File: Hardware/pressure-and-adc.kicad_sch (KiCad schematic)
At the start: 9 parts, among them Q1 Q_NPN_BEC, U6 LWP040-PSGLC-S, U7 ADS1015IDGSR, U8 INA350ABSIDDFR

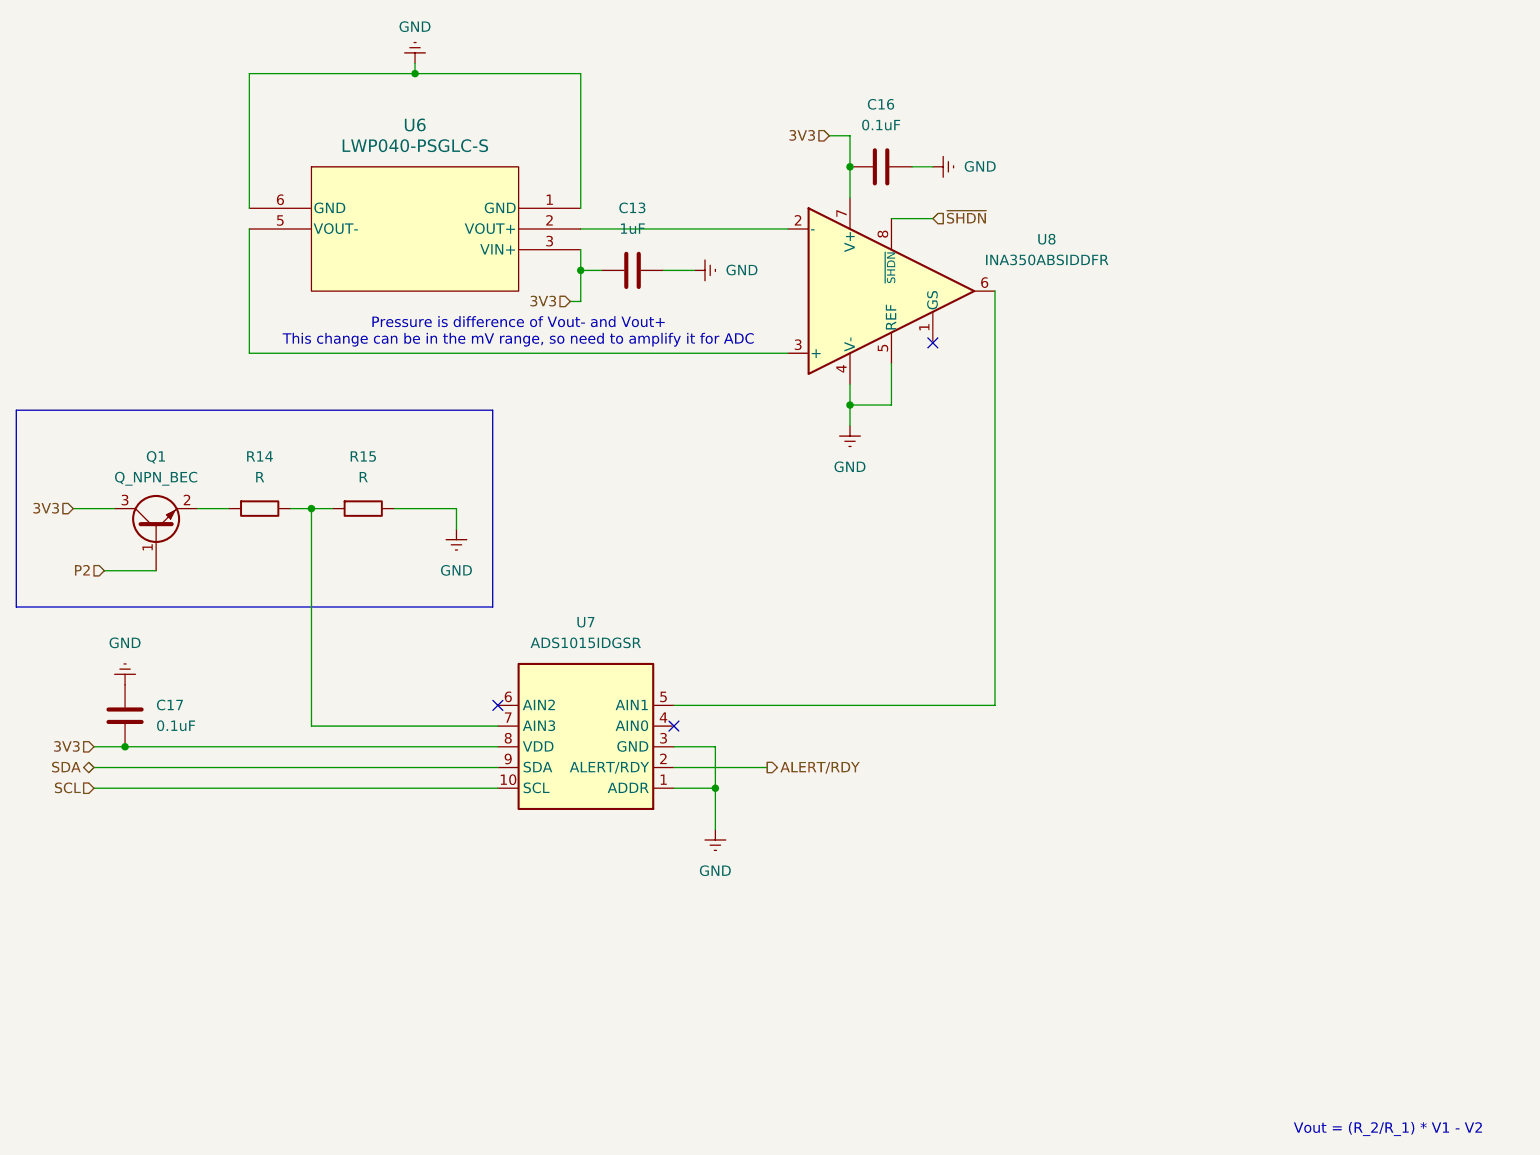
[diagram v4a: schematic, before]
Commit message: Initial OS architecture, and updated PCB work After a joint planning session, designed and architected OS structure: ``` src/ |- os: Audio, Accelerometer, Humidity, etc |- drivers: I2C interfaces, per-chip ```
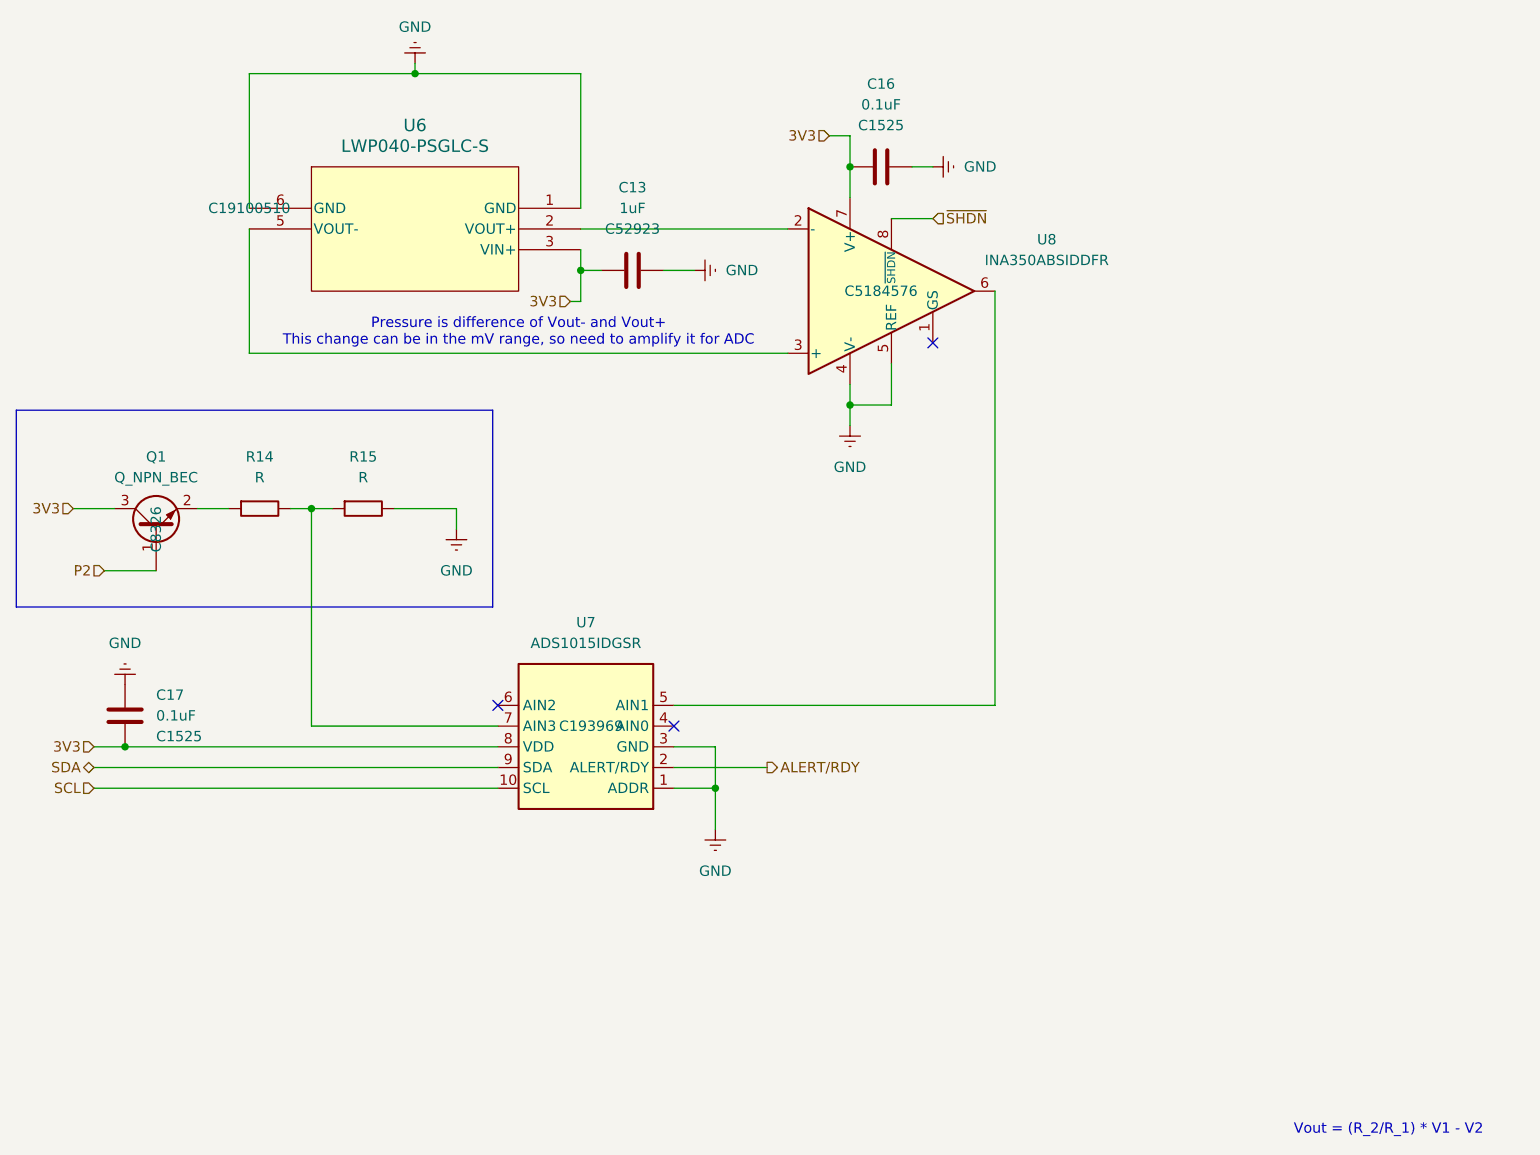
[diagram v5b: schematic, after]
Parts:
- C13: footprint Resistor_SMD:R_01005_0402Metric -> Capacitor_SMD:C_0402_1005Metric; symbol Peanut:C -> Peanut:C 1uF; LCSC (none) -> C52923
- C16, C17: footprint Resistor_SMD:R_01005_0402Metric -> Capacitor_SMD:C_0402_1005Metric; symbol Peanut:C -> Peanut:C 100nF; LCSC (none) -> C1525
- Q1: LCSC (none) -> C8326
- U6: LCSC (none) -> C19100510
- U7: LCSC (none) -> C193969
- U8: LCSC (none) -> C5184576
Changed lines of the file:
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@@
+			)
+		)
+		(property "LCSC" "C5184576"
+			(at 191.77 57.15 0)
+			(effects
+				(font
+					(size 1.27 1.27)
+				)
 			)
 		)
@@
 			)
 		)
+		(property "LCSC" "C19100510"
+			(at 114.3 46.99 0)
+			(effects
+				(font
+					(size 1.27 1.27)
+				)
+			)
+		)
 		(pin "1"
 		)
@@
 	)
 	(symbol
-		(lib_id "Peanut:C")
+		(lib_id "Peanut:C 100nF")
 		(at 99.06 109.22 180)
 		(unit 1)
@@
 		(fields_autoplaced yes)
 		(property "Reference" "C17"
-			(at 102.87 107.9499 0)
+			(at 102.87 106.6799 0)
 			(effects
 				(font
@@
 		)
 		(property "Value" "0.1uF"
-			(at 102.87 110.4899 0)
+			(at 102.87 109.2199 0)
 			(effects
 				(font
@@
 			)
 		)
-		(property "Footprint" "Resistor_SMD:R_01005_0402Metric"
+		(property "Footprint" "Capacitor_SMD:C_0402_1005Metric"
 			(at 98.0948 105.41 0)
 			(effects
@@
 			)
 		)
-		(property "Description" "Unpolarized capacitor"
+		(property "Description" "Capacitor 100nF"
 			(at 99.06 109.22 0)
 			(effects
@@
 				)
 				(hide yes)
+			)
+		)
+		(property "LCSC" "C1525"
+			(at 102.87 111.7599 0)
+			(effects
+				(font
+					(size 1.27 1.27)
+				)
+				(justify right)
 			)
 		)
@@
 			)
 		)
+		(property "LCSC" "C8326"
+			(at 102.87 86.36 0)
+			(effects
+				(font
+					(size 1.27 1.27)
+				)
+			)
+		)
 		(pin "3"
 		)
@@
 	)
 	(symbol
-		(lib_id "Peanut:C")
+		(lib_id "Peanut:C 100nF")
 		(at 191.77 41.91 90)
 		(unit 1)
@@
 		(fields_autoplaced yes)
 		(property "Reference" "C16"
+			(at 191.77 31.75 90)
+			(effects
+				(font
+					(size 1.27 1.27)
+				)
+			)
+		)
+		(property "Value" "0.1uF"
 			(at 191.77 34.29 90)
 			(effects
@@
 			)
 		)
-		(property "Value" "0.1uF"
-			(at 191.77 36.83 90)
-			(effects
-				(font
-					(size 1.27 1.27)
-				)
-			)
-		)
-		(property "Footprint" "Resistor_SMD:R_01005_0402Metric"
+		(property "Footprint" "Capacitor_SMD:C_0402_1005Metric"
 			(at 195.58 40.9448 0)
 			(effects
@@
 			)
 		)
-		(property "Description" "Unpolarized capacitor"
+		(property "Description" "Capacitor 100nF"
 			(at 191.77 41.91 0)
 			(effects
@@
 				)
 				(hide yes)
+			)
+		)
+		(property "LCSC" "C1525"
+			(at 191.77 36.83 90)
+			(effects
+				(font
+					(size 1.27 1.27)
+				)
 			)
 		)
@@
 			)
 		)
+		(property "LCSC" "C193969"
+			(at 156.21 110.49 0)
+			(effects
+				(font
+					(size 1.27 1.27)
+				)
+			)
+		)
 		(pin "7"
 		)
@@
 	)
 	(symbol
-		(lib_id "Peanut:C")
+		(lib_id "Peanut:C 1uF")
 		(at 161.29 54.61 90)
 		(unit 1)
@@
 		(fields_autoplaced yes)
 		(property "Reference" "C13"
+			(at 161.29 44.45 90)
+			(effects
+				(font
+					(size 1.27 1.27)
+				)
+			)
+		)
+		(property "Value" "1uF"
 			(at 161.29 46.99 90)
 			(effects
@@
 			)
 		)
-		(property "Value" "1uF"
-			(at 161.29 49.53 90)
-			(effects
-				(font
-					(size 1.27 1.27)
-				)
-			)
-		)
-		(property "Footprint" "Resistor_SMD:R_01005_0402Metric"
+		(property "Footprint" "Capacitor_SMD:C_0402_1005Metric"
 			(at 165.1 53.6448 0)
 			(effects
@@
 			)
 		)
+		(property "LCSC" "C52923"
+			(at 161.29 49.53 90)
+			(effects
+				(font
+					(size 1.27 1.27)
+				)
+			)
+		)

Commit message: Updates to PCB and ADC Schematics
- Swapped audio jack to correct pin (4P-DIP)
- Add LCSC numbers for all components
- Reroute some sensitive signal traces
- Add Board rev and author
- add 4x M2 mounting holes
- fixup some misc silkscreen, footprints, and component 3d models
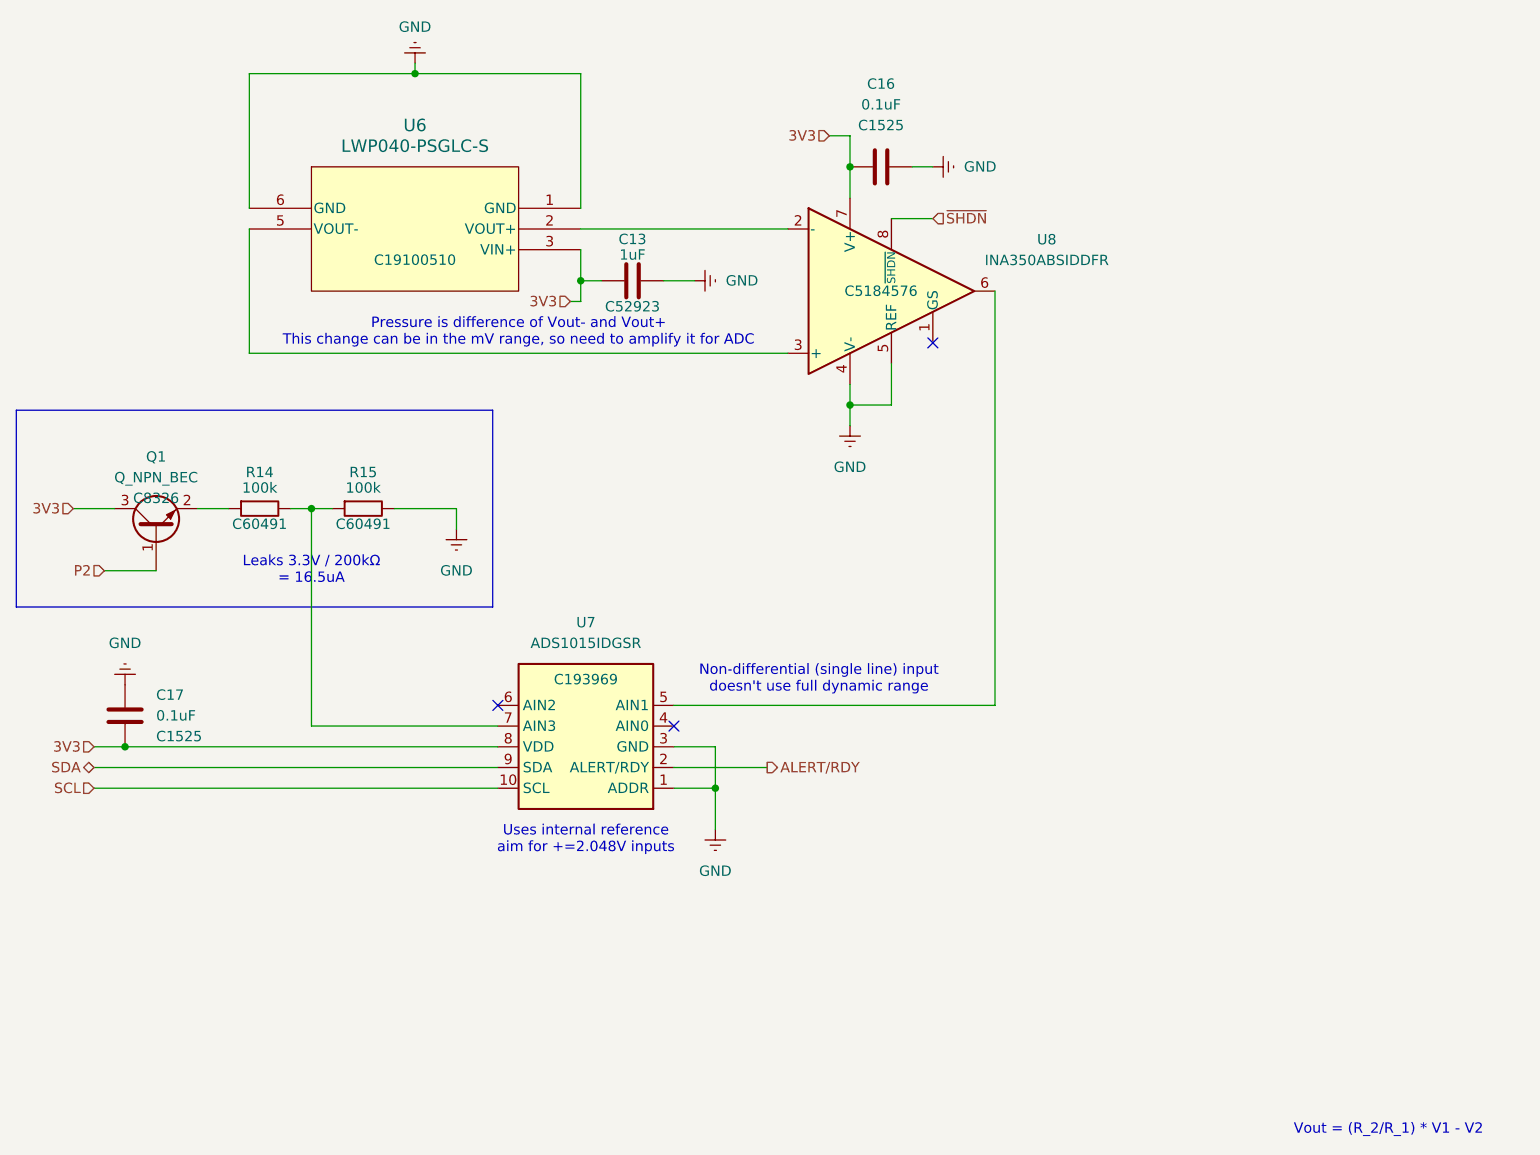
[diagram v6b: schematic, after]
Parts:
- R14, R15: value R -> 100k; symbol Peanut:R -> Peanut:R 100k; LCSC (none) -> C60491
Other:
- note added: "Leaks 3.3V / 200kΩ = 16.5uA"
- note added: "Non-differential (single line) input doesn't use full dynamic range"
- note added: "Uses internal reference aim for +=2.048V inputs"
- moved on the sheet: C13
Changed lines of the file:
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@@
-	)
-	(junction
-		(at 154.94 54.61)
-		(diameter 0)
-		(color 0 0 0 0)
 	)
 	(junction
@@
 	)
 	(junction
+		(at 154.94 55.88)
+		(diameter 0)
+		(color 0 0 0 0)
+	)
+	(junction
 		(at 121.92 83.82)
 		(diameter 0)
@@
 	(wire
 		(pts
+			(xy 154.94 55.88) (xy 154.94 58.42)
+		)
+		(stroke
+			(width 0)
+			(type default)
+		)
+	)
+	(wire
+		(pts
 			(xy 121.92 83.82) (xy 124.46 83.82)
 		)
@@
 	(wire
 		(pts
-			(xy 165.1 54.61) (xy 168.91 54.61)
+			(xy 165.1 55.88) (xy 168.91 55.88)
 		)
 		(stroke
@@
 	(wire
 		(pts
-			(xy 154.94 52.07) (xy 154.94 54.61)
-		)
-		(stroke
-			(width 0)
-			(type default)
-		)
-	)
-	(wire
-		(pts
 			(xy 193.04 48.26) (xy 198.12 48.26)
 		)
@@
 	(wire
 		(pts
-			(xy 154.94 54.61) (xy 157.48 54.61)
+			(xy 154.94 55.88) (xy 157.48 55.88)
 		)
 		(stroke
@@
 	(wire
 		(pts
-			(xy 154.94 54.61) (xy 154.94 58.42)
+			(xy 154.94 52.07) (xy 154.94 55.88)
 		)
 		(stroke
@@
 		(exclude_from_sim no)
 		(at 147.32 62.23 0)
+		(effects
+			(font
+				(size 1.27 1.27)
+			)
+		)
+	)
+	(text "Uses internal reference\naim for +=2.048V inputs"
+		(exclude_from_sim no)
+		(at 155.575 124.46 0)
+		(effects
+			(font
+				(size 1.27 1.27)
+			)
+		)
+	)
+	(text "Non-differential (single line) input\ndoesn't use full dynamic range"
+		(exclude_from_sim no)
+		(at 184.15 104.775 0)
+		(effects
+			(font
+				(size 1.27 1.27)
+			)
+		)
+	)
+	(text "Leaks 3.3V / 200kΩ\n= 16.5uA"
+		(exclude_from_sim no)
+		(at 121.92 91.44 0)
 		(effects
 			(font
@@
 	(symbol
 		(lib_id "Peanut:GND")
-		(at 168.91 54.61 90)
+		(at 168.91 55.88 90)
 		(unit 1)
 		(exclude_from_sim no)
@@
 		(fields_autoplaced yes)
 		(property "Reference" "#PWR033"
-			(at 175.26 54.61 0)
+			(at 175.26 55.88 0)
 			(effects
 				(font
@@
 		)
 		(property "Value" "GND"
-			(at 172.72 54.6099 90)
+			(at 172.72 55.8799 90)
 			(effects
 				(font
@@
 		)
 		(property "Footprint" ""
-			(at 168.91 54.61 0)
+			(at 168.91 55.88 0)
 			(effects
 				(font
@@
 		)
 		(property "Datasheet" ""
-			(at 168.91 54.61 0)
+			(at 168.91 55.88 0)
 			(effects
 				(font
@@
 		)
 		(property "Description" ""
-			(at 177.546 54.61 0)
+			(at 177.546 55.88 0)
 			(effects
 				(font
@@
 		(on_board yes)
 		(dnp no)
-		(fields_autoplaced yes)
 		(property "Reference" "U6"
 			(at 134.62 36.83 0)
@@
 		)
 		(property "LCSC" "C19100510"
-			(at 114.3 46.99 0)
+			(at 134.62 53.34 0)
 			(effects
 				(font
@@
 	)
 	(symbol
-		(lib_id "Peanut:R")
+		(lib_id "Peanut:R 100k")
 		(at 115.57 83.82 0)
 		(unit 1)
@@
 		(on_board yes)
 		(dnp no)
-		(fields_autoplaced yes)
 		(property "Reference" "R14"
-			(at 115.57 77.47 0)
-			(effects
-				(font
-					(size 1.27 1.27)
-				)
-			)
-		)
-		(property "Value" "R"
-			(at 115.57 80.01 0)
+			(at 115.57 79.375 0)
+			(effects
+				(font
+					(size 1.27 1.27)
+				)
+			)
+		)
+		(property "Value" "100k"
+			(at 115.57 81.28 0)
 			(effects
 				(font
@@
 				)
 				(hide yes)
+			)
+		)
+		(property "LCSC" "C60491"
+			(at 115.57 85.725 0)
+			(effects
+				(font
+					(size 1.27 1.27)
+				)
 			)
 		)
@@
 		(on_board yes)
 		(dnp no)
-		(fields_autoplaced yes)
 		(property "Reference" "Q1"
 			(at 102.87 77.47 90)
@@
 		)
 		(property "LCSC" "C8326"
-			(at 102.87 86.36 0)
+			(at 102.87 82.55 90)
 			(effects
 				(font
@@
 	)
 	(symbol
-		(lib_id "Peanut:R")
+		(lib_id "Peanut:R 100k")
 		(at 128.27 83.82 0)
 		(unit 1)
@@
 		(on_board yes)
 		(dnp no)
-		(fields_autoplaced yes)
 		(property "Reference" "R15"
-			(at 128.27 77.47 0)
-			(effects
-				(font
-					(size 1.27 1.27)
-				)
-			)
-		)
-		(property "Value" "R"
-			(at 128.27 80.01 0)
+			(at 128.27 79.375 0)
+			(effects
+				(font
+					(size 1.27 1.27)
+				)
+			)
+		)
+		(property "Value" "100k"
+			(at 128.27 81.28 0)
 			(effects
 				(font
@@
 				)
 				(hide yes)
+			)
+		)
+		(property "LCSC" "C60491"
+			(at 128.27 85.725 0)
+			(effects
+				(font
+					(size 1.27 1.27)
+				)
 			)
 		)
@@
 		(on_board yes)
 		(dnp no)
-		(fields_autoplaced yes)
 		(property "Reference" "U7"
 			(at 155.575 97.79 0)
@@
 		)
 		(property "LCSC" "C193969"
-			(at 156.21 110.49 0)
+			(at 155.575 104.775 0)
 			(effects
 				(font
@@
 	(symbol
 		(lib_id "Peanut:C 1uF")
-		(at 161.29 54.61 90)
+		(at 161.29 55.88 90)
 		(unit 1)
 		(exclude_from_sim no)
@@
 		(on_board yes)
 		(dnp no)
-		(fields_autoplaced yes)
 		(property "Reference" "C13"
-			(at 161.29 44.45 90)
+			(at 161.29 50.8 90)
 			(effects
 				(font
@@
 		)
 		(property "Value" "1uF"
-			(at 161.29 46.99 90)
+			(at 161.29 52.705 90)
 			(effects
 				(font
@@
 		)
 		(property "Footprint" "Capacitor_SMD:C_0402_1005Metric"
-			(at 165.1 53.6448 0)
+			(at 165.1 54.9148 0)
 			(effects
 				(font
@@
 		)
 		(property "Datasheet" "~"
-			(at 161.29 54.61 0)
-			(effects
-				(font
-					(size 1.27 1.27)
-				)
-				(hide yes)
-			)
-		)
-		(property "Description" "Unpolarized capacitor"
-			(at 161.29 54.61 0)
+			(at 161.29 55.88 0)
+			(effects
+				(font
+					(size 1.27 1.27)
+				)
+				(hide yes)
+			)
+		)
+		(property "Description" "Capacitor 1uF"
+			(at 161.29 55.88 0)
 			(effects
 				(font
@@
 		)
 		(property "LCSC" "C52923"
-			(at 161.29 49.53 90)
-			(effects
-				(font
+			(at 161.29 59.055 90)
+			(effects
+				(font
